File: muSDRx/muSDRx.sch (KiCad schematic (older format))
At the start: 105 parts, among them CON1 SJ1-3523N, CON2 SJ1-3523N, J1 Conn_01x02_Male, J11 Conn_01x02_Male, J2 Conn_01x02_Male, J3 Conn_01x02_Male, J4 Conn_01x02_Male, J5 Conn_01x02_Male, J6 Conn_01x02_Male, J9 Conn_01x04_Male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

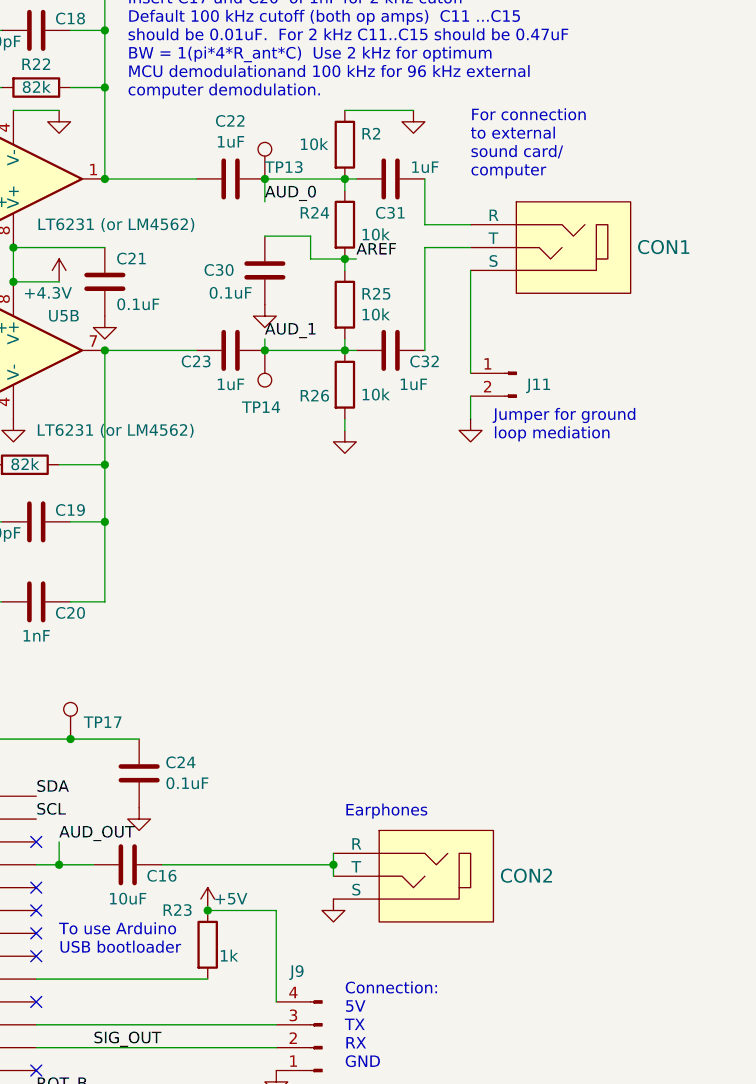
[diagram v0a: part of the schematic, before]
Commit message: Fixed 3.5mm jack footprints so switched ones will work.
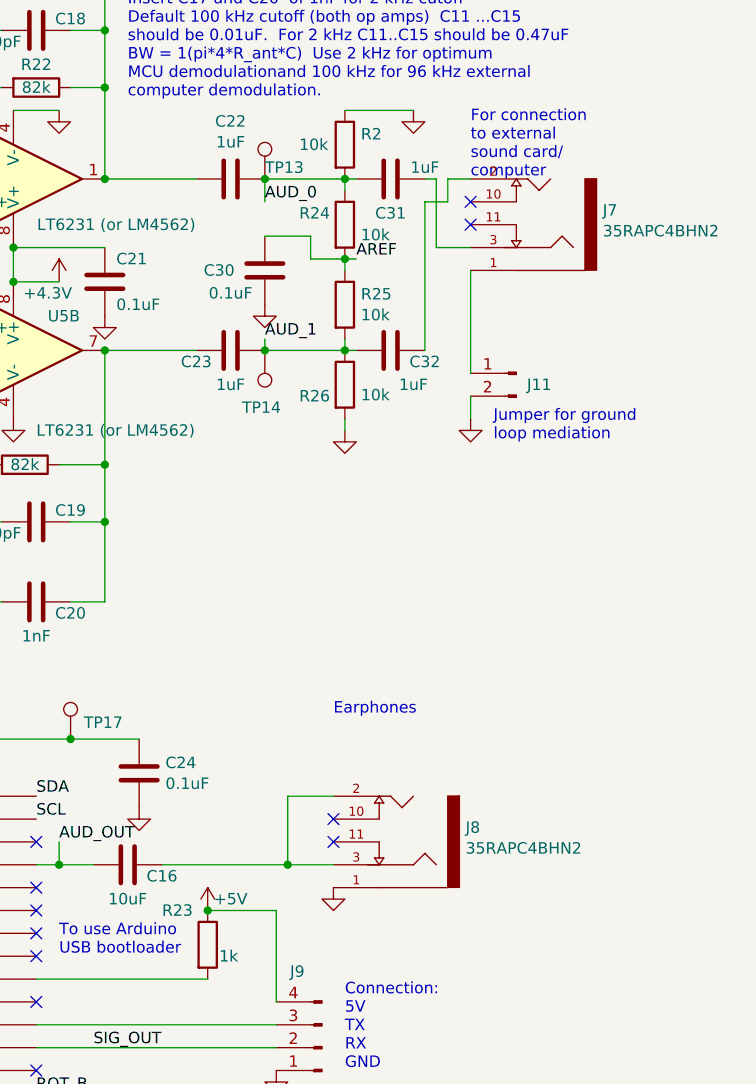
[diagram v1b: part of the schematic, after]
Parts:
- removed CON1, CON2: SJ1-3523N, digikey-footprints:Headphone_Jack_2.5mm_SJ1-3523N, symbol muSDRx-rescue:SJ1-3523N-dk_Barrel-Audio-Connectors
- added J7, J8: 35RAPC4BHN2, SWITCHCRAFT_35RAPC4BHN2, symbol 35RAPC4BHN2:35RAPC4BHN2
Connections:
- net GND: now also J8.1
- net at C16.1: now also J8.2, J8.3
- net at J11.1 (Pin_1): now also J7.1
- net at C32.2: now also J7.2
- net at C31.2: now also J7.3
- no-connect marks 23 -> 27
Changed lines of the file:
@@
 $EndComp
 Wire Wire Line
-	7950 4650 8700 4650
-Wire Wire Line
-	8700 4600 8700 4650
-Wire Wire Line
-	8700 4700 8700 4650
-Connection ~ 8700 4650
+	7950 4650 8500 4650
 $Comp
 L power:GND #PWR060
 U 1 1 5F98D5DE
-P 8700 4800
-F 0 "#PWR060" H 8700 4550 50  0001 C CNN
-F 1 "GND" H 8705 4627 50  0001 C CNN
-F 2 "" H 8700 4800 50  0001 C CNN
-F 3 "" H 8700 4800 50  0001 C CNN
-	1    8700 4800
+P 8700 4750
+F 0 "#PWR060" H 8700 4500 50  0001 C CNN
+F 1 "GND" H 8705 4577 50  0001 C CNN
+F 2 "" H 8700 4750 50  0001 C CNN
+F 3 "" H 8700 4750 50  0001 C CNN
+	1    8700 4750
 	-1   0    0    -1
 $EndComp
-Text Notes 8750 4450 0    50   ~ 0
+Text Notes 8700 4000 0    50   ~ 0
 Earphones
 Wire Wire Line
@@
 NoConn ~ 5900 5950
 NoConn ~ 4350 5300
-$Comp
-L muSDRx-rescue:SJ1-3523N-dk_Barrel-Audio-Connectors CON2
-U 1 1 5F160AB4
-P 9100 4700
-F 0 "CON2" H 8772 4700 60  0000 R CNN
-F 1 "SJ1-3523N" H 8772 4647 60  0001 R CNN
-F 2 "digikey-footprints:Headphone_Jack_2.5mm_SJ1-3523N" H 9300 4900 60  0001 L CNN
-F 3 "https://www.cuidevices.com/product/resource/sj1-352xn.pdf" H 9300 5000 60  0001 L CNN
-F 4 "CP1-3523N-ND" H 9300 5100 60  0001 L CNN "Digi-Key_PN"
-F 5 "SJ1-3523N" H 9300 5200 60  0001 L CNN "MPN"
-F 6 "Connectors, Interconnects" H 9300 5300 60  0001 L CNN "Category"
-F 7 "Barrel - Audio Connectors" H 9300 5400 60  0001 L CNN "Family"
-F 8 "https://www.cui.com/product/resource/digikeypdf/sj1-352xn_series.pdf" H 9300 5500 60  0001 L CNN "DK_Datasheet_Link"
-F 9 "/product-detail/en/cui-inc/SJ1-3523N/CP1-3523N-ND/738689" H 9300 5600 60  0001 L CNN "DK_Detail_Page"
-F 10 "CONN JACK STEREO 3.5MM R/A" H 9300 5700 60  0001 L CNN "Description"
-F 11 "CUI Inc." H 9300 5800 60  0001 L CNN "Manufacturer"
-F 12 "Active" H 9300 5900 60  0001 L CNN "Status"
-	1    9100 4700
-	-1   0    0    -1
-$EndComp
-$Comp
-L muSDRx-rescue:SJ1-3523N-dk_Barrel-Audio-Connectors CON1
-U 1 1 5F1644E0
-P 9700 1950
-F 0 "CON1" H 9372 1950 60  0000 R CNN
-F 1 "SJ1-3523N" H 9372 1897 60  0001 R CNN
-F 2 "digikey-footprints:Headphone_Jack_2.5mm_SJ1-3523N" H 9900 2150 60  0001 L CNN
-F 3 "https://www.cuidevices.com/product/resource/sj1-352xn.pdf" H 9900 2250 60  0001 L CNN
-F 4 "CP1-3523N-ND" H 9900 2350 60  0001 L CNN "Digi-Key_PN"
-F 5 "SJ1-3523N" H 9900 2450 60  0001 L CNN "MPN"
-F 6 "Connectors, Interconnects" H 9900 2550 60  0001 L CNN "Category"
-F 7 "Barrel - Audio Connectors" H 9900 2650 60  0001 L CNN "Family"
-F 8 "https://www.cui.com/product/resource/digikeypdf/sj1-352xn_series.pdf" H 9900 2750 60  0001 L CNN "DK_Datasheet_Link"
-F 9 "/product-detail/en/cui-inc/SJ1-3523N/CP1-3523N-ND/738689" H 9900 2850 60  0001 L CNN "DK_Detail_Page"
-F 10 "CONN JACK STEREO 3.5MM R/A" H 9900 2950 60  0001 L CNN "Description"
-F 11 "CUI Inc." H 9900 3050 60  0001 L CNN "Manufacturer"
-F 12 "Active" H 9900 3150 60  0001 L CNN "Status"
-	1    9700 1950
-	-1   0    0    -1
-$EndComp
 Text Notes 4900 3550 0    50   ~ 0
 See note about BW above to the right.
@@
 	8400 2400 8750 2400
 Connection ~ 8750 2400
-Wire Wire Line
-	9100 2400 9100 1950
-Wire Wire Line
-	9100 1950 9300 1950
-Wire Wire Line
-	9300 1850 9100 1850
-Wire Wire Line
-	9100 1850 9100 1650
 Wire Wire Line
 	8750 2050 8750 2000
@@
 Wire Wire Line
 	7700 2400 8100 2400
+$Comp
+L 35RAPC4BHN2:35RAPC4BHN2 J7
+U 1 1 608B0BD2
+P 9600 1850
+F 0 "J7" H 9322 1787 50  0000 R CNN
+F 1 "35RAPC4BHN2" H 9322 1878 50  0000 R CNN
+F 2 "SWITCHCRAFT_35RAPC4BHN2" H 9600 1850 50  0001 L BNN
+F 3 "" H 9600 1850 50  0001 L BNN
+F 4 "1.01 USD" H 9600 1850 50  0001 L BNN "PRICE"
+F 5 "Manufacturer Recommendation" H 9600 1850 50  0001 L BNN "STANDARD"
+F 6 "None" H 9600 1850 50  0001 L BNN "PACKAGE"
+F 7 "Switchcraft" H 9600 1850 50  0001 L BNN "MF"
+F 8 "Conn 3.5MM Stereo Jack F 5 POS Solder RA Thru-Hole 5 Terminal 1 Port" H 9600 1850 50  0001 L BNN "DESCRIPTION"
+F 9 "Good" H 9600 1850 50  0001 L BNN "AVAILABILITY"
+F 10 "35RAPC4BHN2" H 9600 1850 50  0001 L BNN "MP"
+	1    9600 1850
+	-1   0    0    1
+$EndComp
+NoConn ~ 9300 1750
+NoConn ~ 9300 1850
+$Comp
+L 35RAPC4BHN2:35RAPC4BHN2 J8
+U 1 1 608F6A1C
+P 9000 4550
+F 0 "J8" H 8722 4487 50  0000 R CNN
+F 1 "35RAPC4BHN2" H 8722 4578 50  0000 R CNN
+F 2 "SWITCHCRAFT_35RAPC4BHN2" H 9000 4550 50  0001 L BNN
+F 3 "" H 9000 4550 50  0001 L BNN
+F 4 "1.01 USD" H 9000 4550 50  0001 L BNN "PRICE"
+F 5 "Manufacturer Recommendation" H 9000 4550 50  0001 L BNN "STANDARD"
+F 6 "None" H 9000 4550 50  0001 L BNN "PACKAGE"
+F 7 "Switchcraft" H 9000 4550 50  0001 L BNN "MF"
+F 8 "Conn 3.5MM Stereo Jack F 5 POS Solder RA Thru-Hole 5 Terminal 1 Port" H 9000 4550 50  0001 L BNN "DESCRIPTION"
+F 9 "Good" H 9000 4550 50  0001 L BNN "AVAILABILITY"
+F 10 "35RAPC4BHN2" H 9000 4550 50  0001 L BNN "MP"
+	1    9000 4550
+	-1   0    0    1
+$EndComp
+NoConn ~ 8700 4450
+NoConn ~ 8700 4550
+Wire Wire Line
+	8700 4350 8500 4350
+Wire Wire Line
+	8500 4350 8500 4650
+Connection ~ 8500 4650
+Wire Wire Line
+	8500 4650 8700 4650
+Wire Wire Line
+	9100 1650 9150 1650
+Wire Wire Line
+	9150 1650 9150 1950
+Wire Wire Line
+	9150 1950 9300 1950
+Wire Wire Line
+	9100 1750 9200 1750
+Wire Wire Line
+	9200 1750 9200 1650
+Wire Wire Line
+	9200 1650 9300 1650
+Wire Wire Line
+	9100 1750 9100 2400
 $EndSCHEMATC

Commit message: So I could change branches.
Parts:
- J7, J8: symbol 35RAPC4BHN2:35RAPC4BHN2 -> muSDRx-rescue:35RAPC4BHN2-35RAPC4BHN2
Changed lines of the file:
@@
 	7700 2400 8100 2400
 $Comp
-L 35RAPC4BHN2:35RAPC4BHN2 J7
+L muSDRx-rescue:35RAPC4BHN2-35RAPC4BHN2 J7
 U 1 1 608B0BD2
 P 9600 1850
@@
 NoConn ~ 9300 1850
 $Comp
-L 35RAPC4BHN2:35RAPC4BHN2 J8
+L muSDRx-rescue:35RAPC4BHN2-35RAPC4BHN2 J8
 U 1 1 608F6A1C
 P 9000 4550
